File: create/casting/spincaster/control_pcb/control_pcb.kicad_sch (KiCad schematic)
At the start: 10 parts, among them J1 Extra, J2 Buzzer, J3 Relay, J4 FET, J5 Rocker, J6 PWR, SW2 IND_OFF, SW3 IND_ON, SW4 IND_PULSE

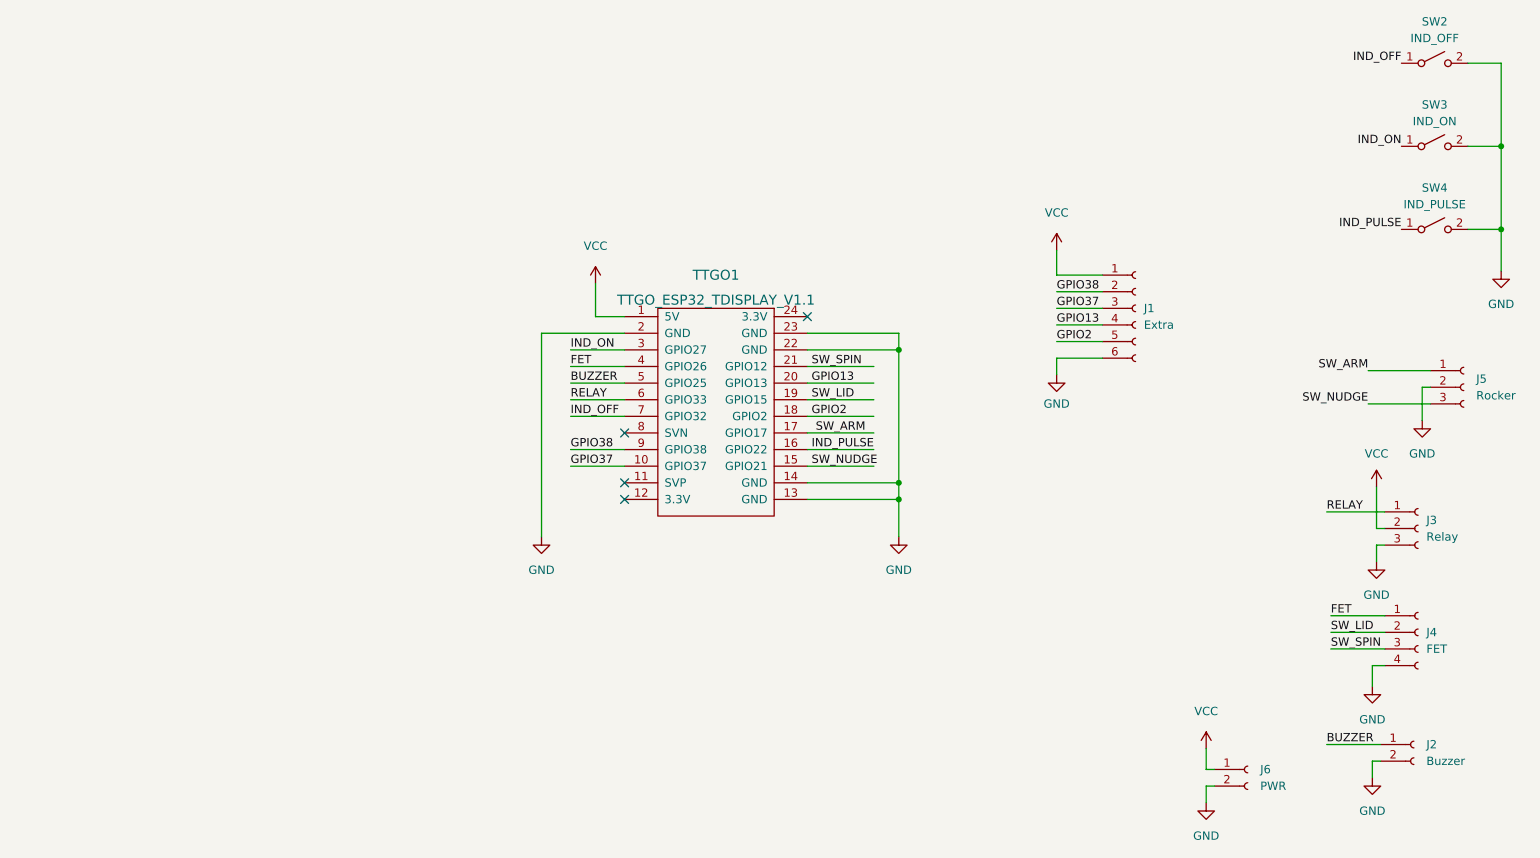
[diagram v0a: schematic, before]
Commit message: Better touch-mark, added mixer float notebook, some mods to spincaster control
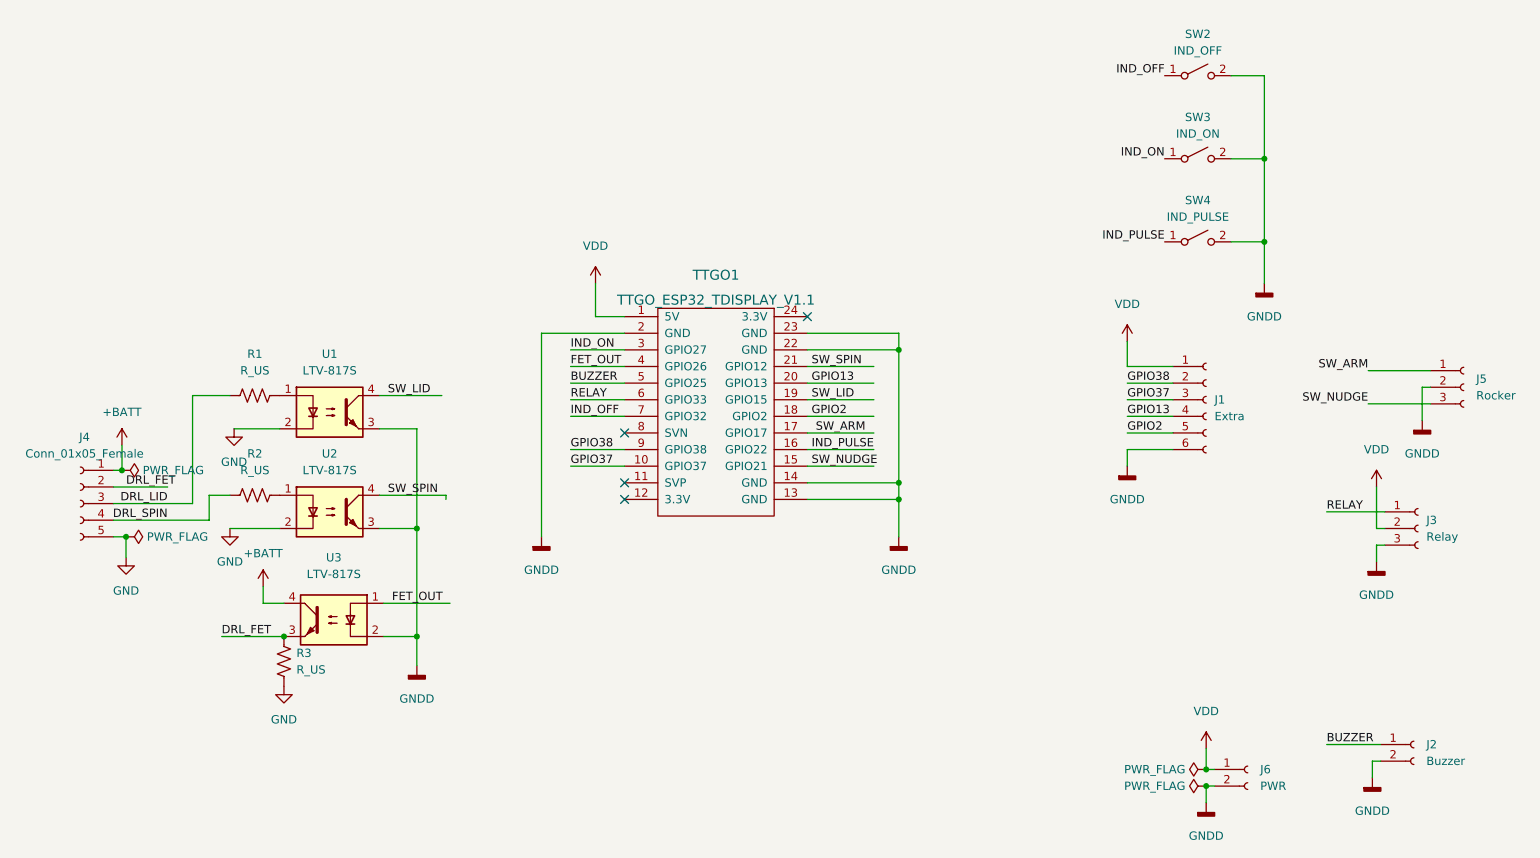
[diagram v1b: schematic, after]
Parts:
- removed J4: FET, Connector_JST:JST_PH_B4B-PH-K_1x04_P2.00mm_Vertical, symbol Connector:Conn_01x04_Female
- added J4: Conn_01x05_Female, Connector_Molex:Molex_KK-254_AE-6410-05A_1x05_P2.54mm_Vertical, symbol Connector:Conn_01x05_Female
- added R1, R2, R3: R_US, Resistor_SMD:R_0805_2012Metric, symbol Device:R_US
- added U1, U2, U3: LTV-817S, Package_DIP:SMDIP-4_W9.53mm, symbol Isolator:LTV-817S
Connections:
- net GND: now also J4.5 (Pin_5), R3.2, U1.2, U2.2; no longer J1.6 (Pin_6), J2.2 (Pin_2), J3.3 (Pin_3), J5.2 (Pin_2), J6.2 (Pin_2), SW2.2 (B), SW3.2 (B), SW4.2 (B), TTGO1.13 (GND), TTGO1.14 (GND), TTGO1.2 (GND), TTGO1.22 (GND), TTGO1.23 (GND)
- net SW_LID: now also U1.4
- net SW_SPIN: now also U2.4
- net FET renamed FET_OUT
- net FET_OUT: now also U3.1
- net VCC renamed VDD
- new net: R1.2, U1.1
- new net: R2.2, U2.1
- new net +BATT: J4.1 (Pin_1), U3.4
- new net DRL_FET: J4.2 (Pin_2), R3.1, U3.3
- new net DRL_LID: J4.3 (Pin_3), R1.1
- new net DRL_SPIN: J4.4 (Pin_4), R2.1
- new net GNDD: J1.6 (Pin_6), J2.2 (Pin_2), J3.3 (Pin_3), J5.2 (Pin_2), J6.2 (Pin_2), SW2.2 (B), SW3.2 (B), SW4.2 (B), TTGO1.13 (GND), TTGO1.14 (GND), TTGO1.2 (GND), TTGO1.22 (GND), TTGO1.23 (GND), U1.3, U2.3, U3.2
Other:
- moved on the sheet: J1, SW2, SW3, SW4
